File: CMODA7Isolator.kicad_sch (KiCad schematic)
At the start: 35 parts, among them J1 Conn_01x24, J2 Conn_01x24, M1 Artix_7_35T_CMOD_A7, U1 TXB0108, U2 TXB0108, U3 TXB0108, U4 TXB0108, U5 TXB0108, U6 TXB0108, U7 LD1117S33TR_SOT223

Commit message: Test of branching
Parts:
- added D?: D_Schottky, Diode_SMD:D_SOD-123, symbol Device:D_Schottky
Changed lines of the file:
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@@
     (pin "1")
+  )
+  (symbol (lib_id "Device:D_Schottky") (at 146.685 41.91 270) (unit 1)
+    (in_bom yes) (on_board yes) (fields_autoplaced)
+    (property "Reference" "D?" (id 0) (at 149.86 40.3224 90)
+      (effects (font (size 1.27 1.27)) (justify left))
+    )
+    (property "Value" "D_Schottky" (id 1) (at 149.86 42.8624 90)
+      (effects (font (size 1.27 1.27)) (justify left))
+    )
+    (property "Footprint" "Diode_SMD:D_SOD-123" (id 2) (at 146.685 41.91 0)
+      (effects (font (size 1.27 1.27)) hide)
+    )
+    (property "Datasheet" "~" (id 3) (at 146.685 41.91 0)
+      (effects (font (size 1.27 1.27)) hide)
+    )
+    (pin "1")
+    (pin "2")
   )
   (symbol (lib_id "Device:C_Small") (at 118.11 110.49 0) (unit 1)
@@
       (reference "D5") (unit 1) (value "LED") (footprint "LED_SMD:LED_0603_1608Metric")
     )
+    (path "/7d118989-8d72-41d5-912e-d242ec0b54a4"
+      (reference "D?") (unit 1) (value "D_Schottky") (footprint "Diode_SMD:D_SOD-123")
+    )
     (path "/e69e1a2f-80a8-4128-bfcd-b34abab4e68c"

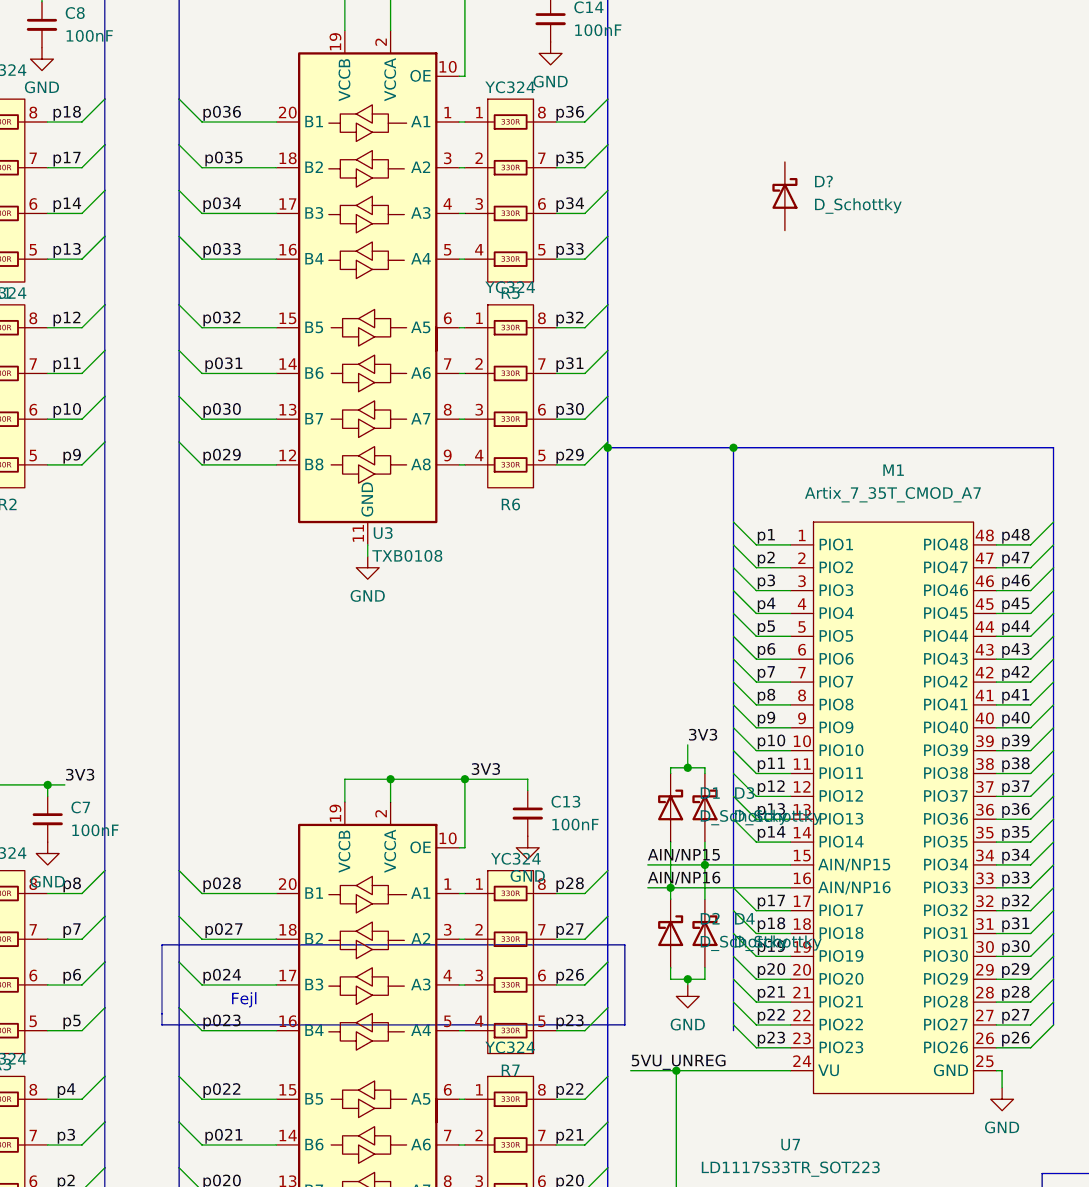
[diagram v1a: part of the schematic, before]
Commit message: Fixed Issue #3
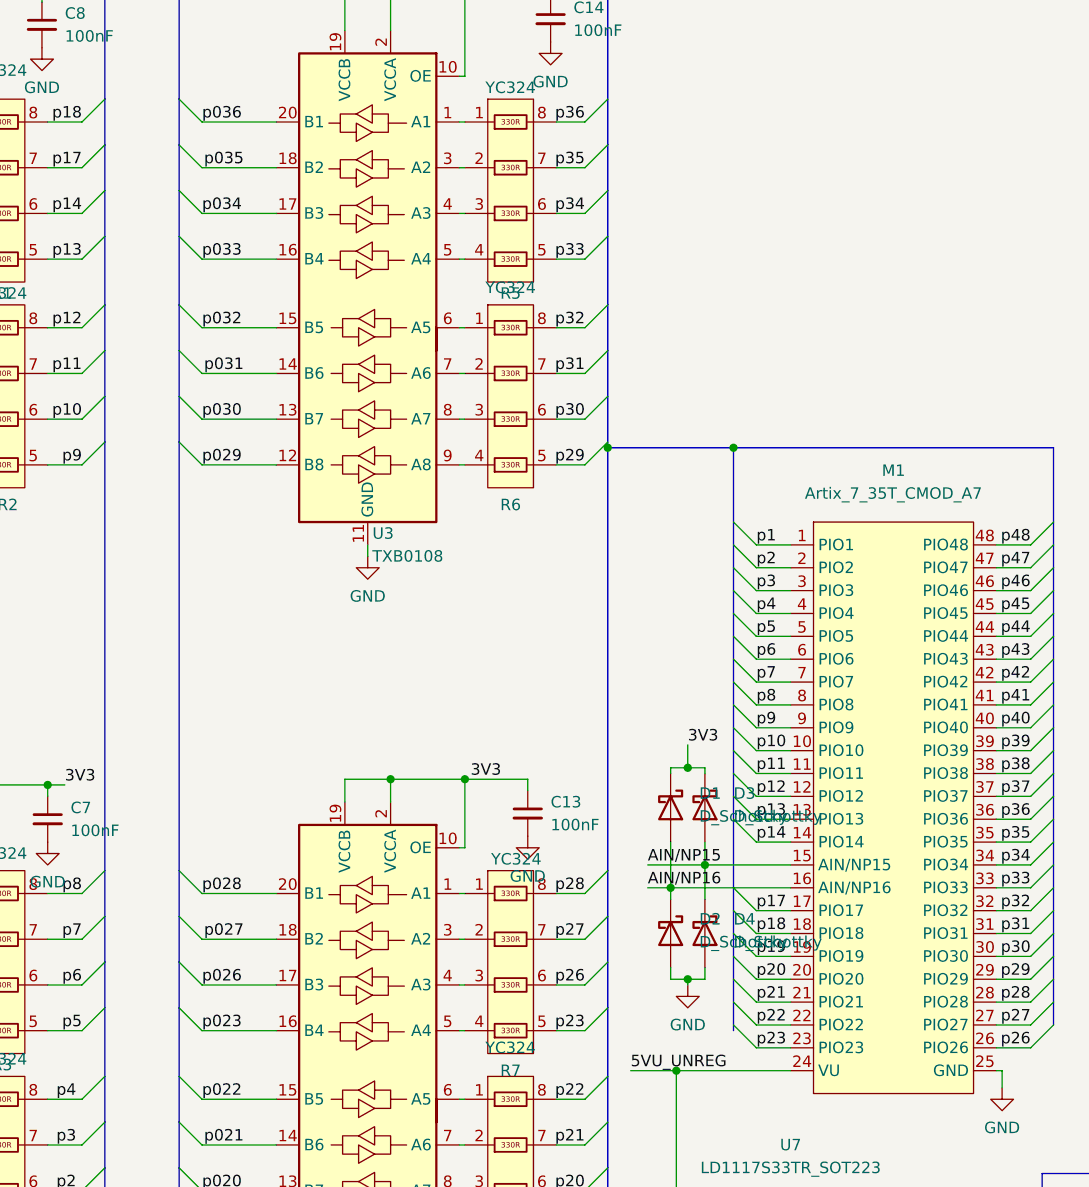
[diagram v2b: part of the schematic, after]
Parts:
- removed D?: D_Schottky, Diode_SMD:D_SOD-123, symbol Device:D_Schottky
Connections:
- net p024 is gone; now on net p026: U4.17 (B3)
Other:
- note removed: "Fejl"
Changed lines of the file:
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@@
     (stroke (width 0) (type default) (color 0 0 0 0))
   )
-  (polyline (pts (xy 128.905 125.095) (xy 128.905 133.985))
-    (stroke (width 0) (type default) (color 0 0 0 0))
-  )
   (wire (pts (xy 260.985 143.51) (xy 259.715 143.51))
     (stroke (width 0) (type default) (color 0 0 0 0))
@@
     (stroke (width 0) (type default) (color 0 0 0 0))
   )
-  (polyline (pts (xy 77.47 125.095) (xy 128.905 125.095))
-    (stroke (width 0) (type default) (color 0 0 0 0))
-  )
   (wire (pts (xy 247.65 138.43) (xy 260.985 138.43))
     (stroke (width 0) (type default) (color 0 0 0 0))
@@
     (stroke (width 0) (type default) (color 0 0 0 0))
   )
-  (polyline (pts (xy 128.905 133.985) (xy 77.47 133.985))
-    (stroke (width 0) (type default) (color 0 0 0 0))
-  )
   (wire (pts (xy 46.355 107.315) (xy 46.355 109.22))
     (stroke (width 0) (type default) (color 0 0 0 0))
@@
     (stroke (width 0) (type default) (color 0 0 0 0))
   )
-  (polyline (pts (xy 77.47 132.715) (xy 77.47 133.985))
-    (stroke (width 0) (type default) (color 0 0 0 0))
-  )
   (bus (pts (xy 23.495 144.78) (xy 23.495 139.7))
     (stroke (width 0) (type default) (color 255 22 26 1))
@@
     (stroke (width 0) (type default) (color 0 0 0 0))
   )
-  (polyline (pts (xy 77.47 132.715) (xy 77.47 125.095))
-    (stroke (width 0) (type default) (color 0 0 0 0))
-  )
   (wire (pts (xy 143.51 95.885) (xy 147.32 95.885))
     (stroke (width 0) (type default) (color 0 0 0 0))
@@
     (effects (font (size 1.27 1.27)) (justify left bottom))
   )
-  (text "Fejl\n" (at 85.09 132.08 0)
-    (effects (font (size 1.27 1.27)) (justify left bottom))
-  )
   (label "p04" (at 26.035 142.24 0)
     (effects (font (size 1.27 1.27)) (justify left bottom))
@@
     (effects (font (size 1.27 1.27)) (justify right bottom))
   )
-  (label "p024" (at 81.915 129.54 0)
+  (label "p026" (at 81.915 129.54 0)
     (effects (font (size 1.27 1.27)) (justify left bottom))
   )
@@
     (pin "1")
   )
-  (symbol (lib_id "Device:D_Schottky") (at 146.685 41.91 270) (unit 1)
-    (in_bom yes) (on_board yes) (fields_autoplaced)
-    (property "Reference" "D?" (id 0) (at 149.86 40.3224 90)
-      (effects (font (size 1.27 1.27)) (justify left))
-    )
-    (property "Value" "D_Schottky" (id 1) (at 149.86 42.8624 90)
-      (effects (font (size 1.27 1.27)) (justify left))
-    )
-    (property "Footprint" "Diode_SMD:D_SOD-123" (id 2) (at 146.685 41.91 0)
-      (effects (font (size 1.27 1.27)) hide)
-    )
-    (property "Datasheet" "~" (id 3) (at 146.685 41.91 0)
-      (effects (font (size 1.27 1.27)) hide)
-    )
-    (pin "1")
-    (pin "2")
-  )
   (symbol (lib_id "Device:C_Small") (at 118.11 110.49 0) (unit 1)
     (in_bom yes) (on_board yes) (fields_autoplaced)
@@
       (reference "D5") (unit 1) (value "LED") (footprint "LED_SMD:LED_0603_1608Metric")
     )
-    (path "/7d118989-8d72-41d5-912e-d242ec0b54a4"
-      (reference "D?") (unit 1) (value "D_Schottky") (footprint "Diode_SMD:D_SOD-123")
-    )
     (path "/e69e1a2f-80a8-4128-bfcd-b34abab4e68c"

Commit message: Issue #6 fixed
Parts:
- removed C1, C13, C14, C22, C24, C7, C8: 100nF, Capacitor_SMD:C_0805_2012Metric_Pad1.18x1.45mm_HandSolder, symbol Device:C_Small
- removed C2: 10uF, Capacitor_SMD:C_0805_2012Metric_Pad1.18x1.45mm_HandSolder, symbol Device:C_Small
- removed D1, D2, D3, D4: D_Schottky, Diode_SMD:D_SOD-123, symbol Device:D_Schottky
- removed D5: LED, LED_SMD:LED_0603_1608Metric, symbol Device:LED
- removed J1, J2: Conn_01x24, Connector_PinHeader_2.54mm:PinHeader_1x24_P2.54mm_Vertical, symbol Connector_Generic:Conn_01x24
- removed M1: Artix_7_35T_CMOD_A7, JRIX FPGA:CMOD A7 Module, symbol JRIX FPGA:Artix_7_35T_CMOD_A7
- removed R1, R10, R11, R2, R3, R4, R5, R6, R7, R8, R9: YC324, JRIX Resistor Array Footprints:YC-TC 124 8Pin-4R, symbol JRIX Resistor Array:YC324
- removed R12: 560R, Resistor_SMD:R_0805_2012Metric_Pad1.20x1.40mm_HandSolder, symbol Device:R_Small
- removed U1, U2, U3, U4, U5, U6: TXB0108, Package_SO:TSSOP-20_4.4x6.5mm_P0.65mm, symbol JRIX Level Translator:TXB0108
- removed U7: LD1117S33TR_SOT223, Package_TO_SOT_SMD:SOT-223-3_TabPin2, symbol Regulator_Linear:LD1117S33TR_SOT223
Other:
- added sheet IO (IO.kicad_sch)
- added sheet Supply (Supply.kicad_sch)
- added sheet VABCheck (VABCheck.kicad_sch)
- note removed: "I/O max 10mA jvf. https://docs.xilinx.com/v/u/en-US/ds181_Artix_7_Data_Sheet 3.3/10mA = 330R"
- note removed: "IC har interne pull-ups"
